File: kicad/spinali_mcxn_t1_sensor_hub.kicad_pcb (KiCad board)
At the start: 6 copper layers, 36.5 x 46 mm, 204 parts, among them J1 5055780421, J10 SDO, J11 CKO, J12 GND, J2 USB4105-GF-A, J3 CAN0A, J4 CAN0B, J5 Debug, J6 CAN1A, J7 CAN1B, J8 DF40TC(3.0)-50DP-0.4V(51), J9 DF40TC(3.0)-50DP-0.4V(51), Q1 BUK6D56-60EX, SW1 SW_SPST, U1 LM74700, U10 BMM350, U11 BMP581, U12 TJA1462ATK, U13 TJA1462ATK, U14 SK9822-EC20, U15 TJA1103AHN, U2 NX5P3363UKZ, U3 LM5160DNTJ, U4 NX5P3363UKZ, U5 MIC5504-1.8YMT, U6 MPM3811GG-Z, U7 MCXN947VDFT, U8 PCMF1USB3SZ, U9 ICM-45686, Y1 24MHz, Y2 32.768kHz, Y3 25MHz

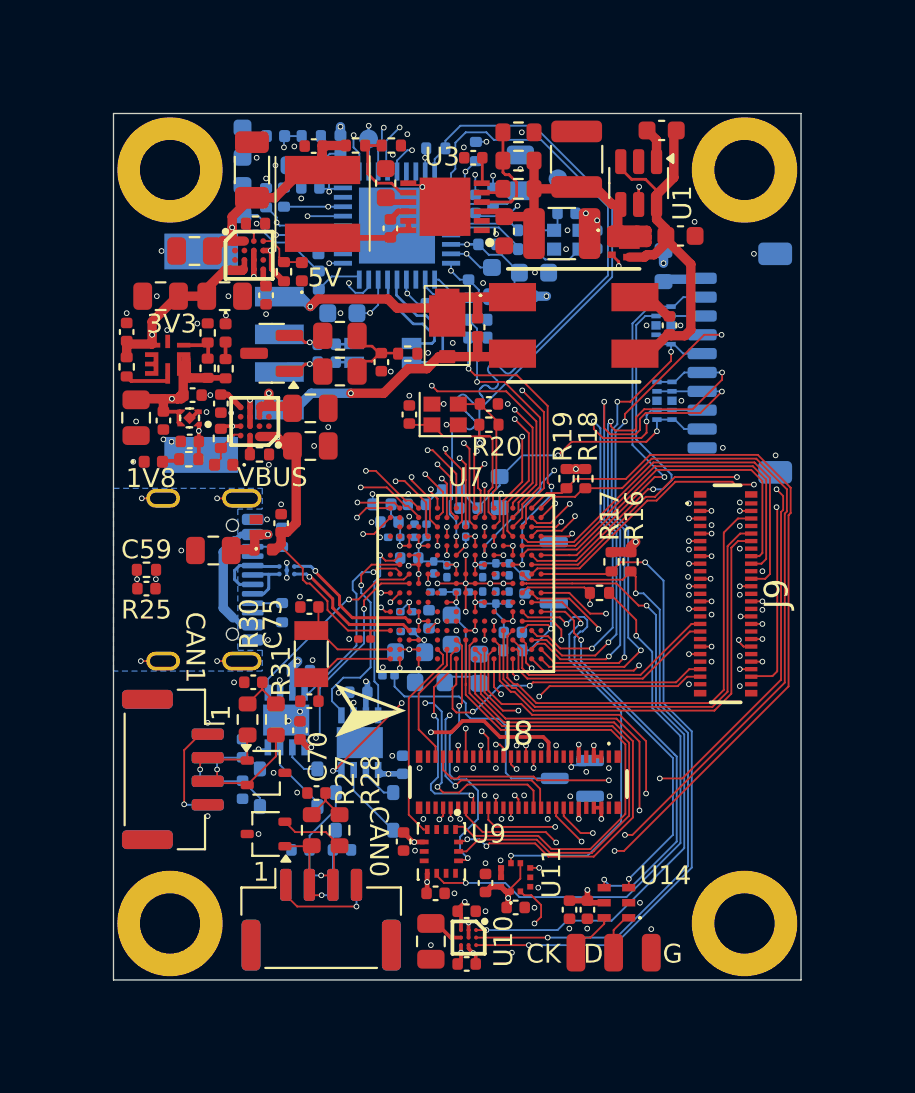
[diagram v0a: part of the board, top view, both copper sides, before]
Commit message: Updated layout and BOM
- Rounded corners of PCB
- Updated board-to-board MFPN to correct one.
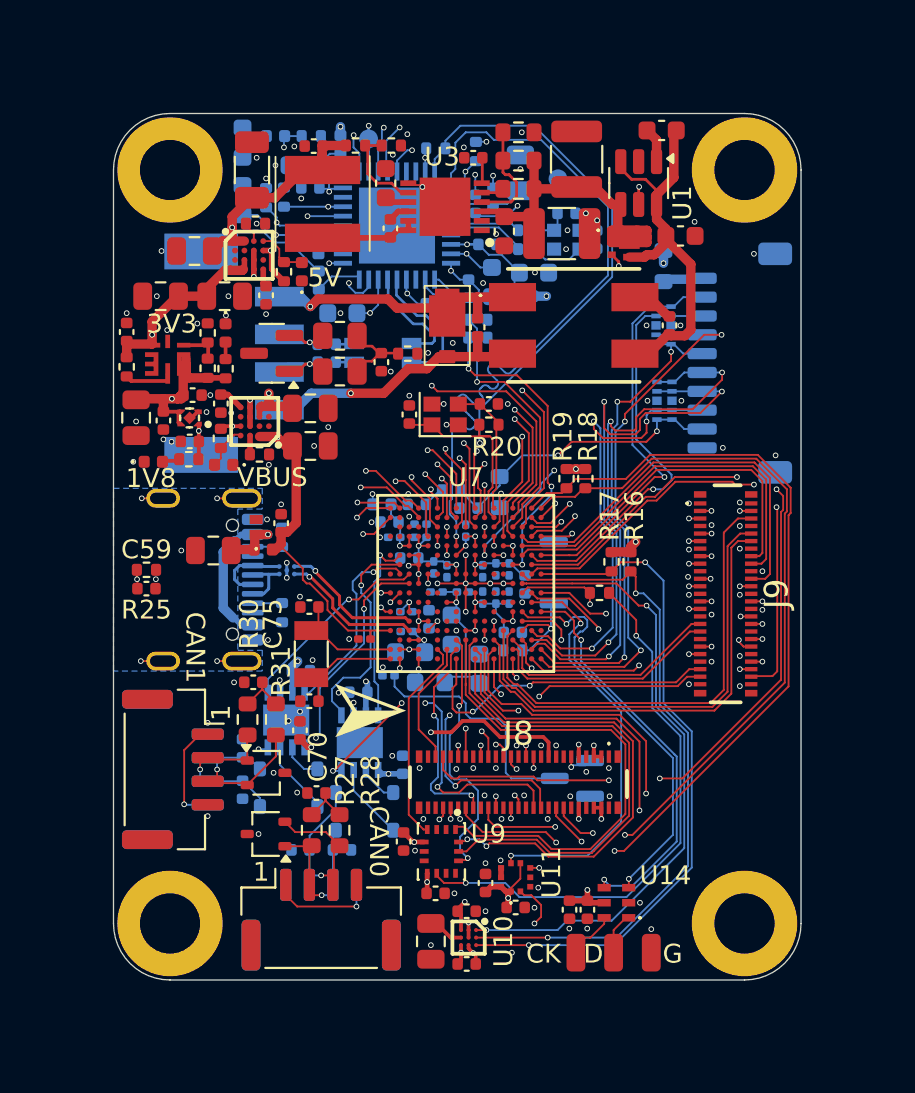
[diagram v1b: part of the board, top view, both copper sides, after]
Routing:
- net +1V8: track 48.1 -> 48.7 mm
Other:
- outline, holes or cut-outs redrawn
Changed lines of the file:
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@@
 		)
 	)
-	(gr_rect
-		(start 82.2 75.95)
-		(end 118.7 121.95)
+	(gr_arc
+		(start 82.2 78.95)
+		(mid 83.07868 76.82868)
+		(end 85.2 75.95)
+		(stroke
+			(width 0.05)
+			(type default)
+		)
+		(layer "Edge.Cuts")
+	)
+	(gr_line
+		(start 115.7 121.95)
+		(end 85.2 121.95)
+		(stroke
+			(width 0.05)
+			(type default)
+		)
+		(layer "Edge.Cuts")
+	)
+	(gr_arc
+		(start 85.2 121.95)
+		(mid 83.07868 121.07132)
+		(end 82.2 118.95)
+		(stroke
+			(width 0.05)
+			(type default)
+		)
+		(layer "Edge.Cuts")
+	)
+	(gr_line
+		(start 85.2 75.95)
+		(end 115.7 75.95)
+		(stroke
+			(width 0.05)
+			(type default)
+		)
+		(layer "Edge.Cuts")
+	)
+	(gr_arc
+		(start 115.7 75.95)
+		(mid 117.82132 76.82868)
+		(end 118.7 78.95)
+		(stroke
+			(width 0.05)
+			(type default)
+		)
+		(layer "Edge.Cuts")
+	)
+	(gr_line
+		(start 118.7 78.95)
+		(end 118.7 118.95)
+		(stroke
+			(width 0.05)
+			(type default)
+		)
+		(layer "Edge.Cuts")
+	)
+	(gr_arc
+		(start 118.7 118.95)
+		(mid 117.82132 121.07132)
+		(end 115.7 121.95)
+		(stroke
+			(width 0.05)
+			(type default)
+		)
+		(layer "Edge.Cuts")
+	)
+	(gr_line
+		(start 82.2 118.95)
+		(end 82.2 78.95)
 		(stroke
 			(width 0.05)
 			(type default)
 		)
-		(fill none)
 		(layer "Edge.Cuts")
 	)
@@
 	)
 	(segment
+		(start 97.25 109.5)
+		(end 97.5 109.5)
+		(width 0.2)
+		(layer "In2.Cu")
+		(net 8)
+	)
+	(segment
 		(start 100.25 116.734314)
 		(end 100.25 116.05)
@@
 	)
 	(segment
+		(start 97.5 109.7)
+		(end 97.5 109.5)
+		(width 0.2)
+		(layer "In2.Cu")
+		(net 8)
+	)
+	(segment
+		(start 97.5 113.3)
+		(end 97.5 109.7)
+		(width 0.2)
+		(layer "In2.Cu")
+		(net 8)
+	)
+	(segment
+		(start 97.7 109.5)
+		(end 97.5 109.5)
+		(width 0.2)
+		(layer "In2.Cu")
+		(net 8)
+	)
+	(segment
 		(start 87.15 94.55)
 		(end 87.15 105.55)
@@
 	(segment
 		(start 94.05 109.5)
-		(end 97.5 109.5)
+		(end 97.25 109.5)
+		(width 0.2)
+		(layer "In2.Cu")
+		(net 8)
+	)
+	(segment
+		(start 98.35 109.5)
+		(end 97.7 109.5)
 		(width 0.2)
 		(layer "In2.Cu")
@@
 	)
 	(segment
+		(start 97.5 109.7)
+		(end 97.3 109.5)
+		(width 0.2)
+		(layer "In2.Cu")
+		(net 8)
+	)
+	(segment
 		(start 87.15 105.55)
 		(end 90.25 108.65)
@@
 	)
 	(segment
-		(start 98.35 109.5)
-		(end 97.5 109.5)
+		(start 97.5 109.7)
+		(end 97.7 109.5)
+		(width 0.2)
+		(layer "In2.Cu")
+		(net 8)
+	)
+	(segment
+		(start 97.3 109.5)
+		(end 97.25 109.5)
 		(width 0.2)
 		(layer "In2.Cu")
@@
 	)
 	(segment
-		(start 97.5 113.3)
-		(end 97.5 109.5)
-		(width 0.2)
-		(layer "In2.Cu")
-		(net 8)
-	)
-	(segment
 		(start 93.2 108.65)
 		(end 94.05 109.5)
@@
 	)
 	(segment
-		(start 108.25 118.97)
-		(end 108.25 118.65)
-		(width 0.1)
-		(layer "F.Cu")
-		(net 224)
-	)
-	(segment
-		(start 107.2 119.7)
-		(end 107.52 119.7)
+		(start 107.52 119.7)
+		(end 108.25 118.97)
 		(width 0.1)
 		(layer "F.Cu")
@@
 	)
 	(segment
-		(start 106.75 120.5)
-		(end 106.75 120.15)
+		(start 108.25 118.97)
+		(end 108.25 118.65)
 		(width 0.1)
 		(layer "F.Cu")
@@
 	)
 	(segment
-		(start 107.52 119.7)
-		(end 108.25 118.97)
+		(start 107.2 119.7)
+		(end 107.52 119.7)
 		(width 0.1)
 		(layer "F.Cu")
@@
 	)
 	(segment
-		(start 108.25 118.97)
-		(end 108.25 118.9)
+		(start 106.75 120.15)
+		(end 107.2 119.7)
 		(width 0.1)
 		(layer "F.Cu")
@@
 	)
 	(segment
-		(start 106.75 120.15)
-		(end 107.2 119.7)
+		(start 106.75 120.5)
+		(end 106.75 120.15)
 		(width 0.1)
 		(layer "F.Cu")

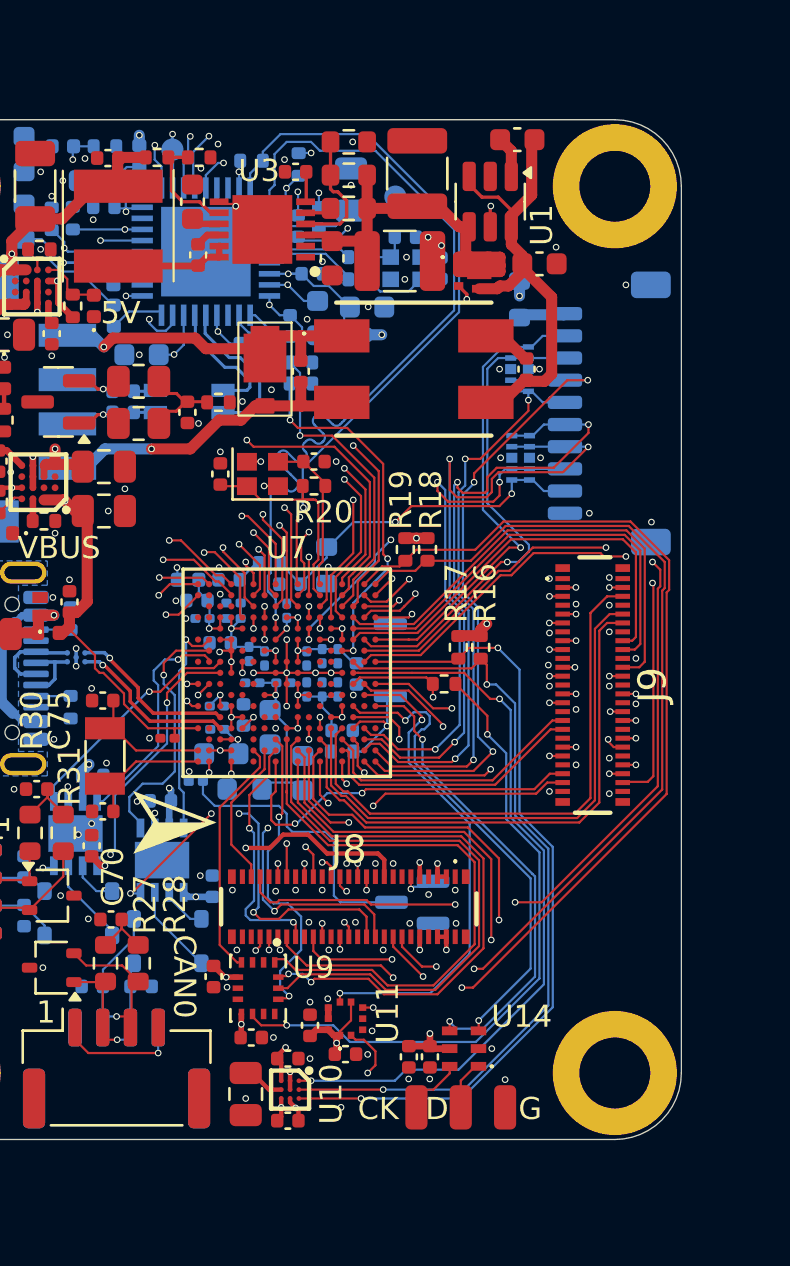
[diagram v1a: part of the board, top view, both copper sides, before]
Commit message: Updated PCB layout
- Changed North vector symbol on silk to an XYZ axis symbol.
- Flipped magnetometer to bottom side to have orientation match the IMU.
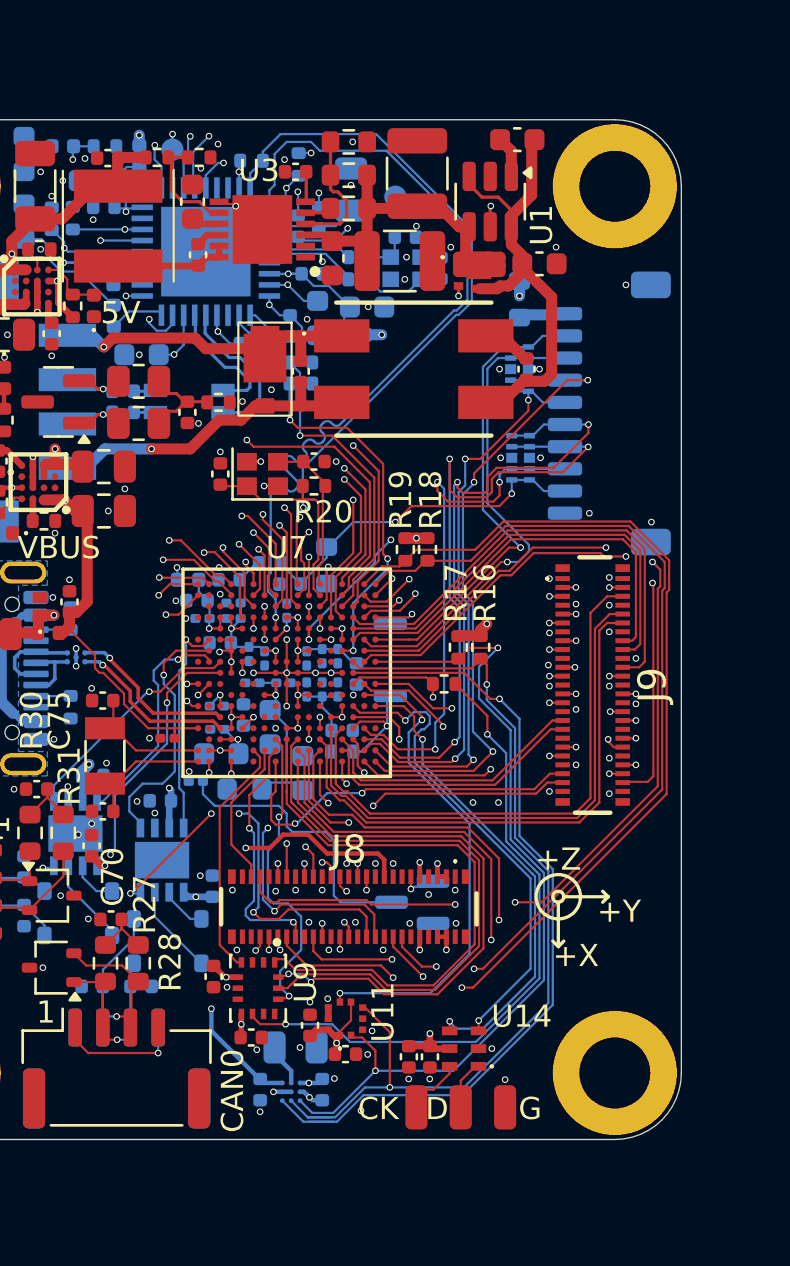
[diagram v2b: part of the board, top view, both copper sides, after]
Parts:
- removed the G*** at (95.8, 107.7)
- C62, C63, C64, U10: moved to B.Cu
- moved C64 3.08 mm to (101.3, 117.8), turned to 0 degrees
- moved C62 2.09 mm to (102.5, 119.7), turned to 90 degrees
- moved C63 1.88 mm to (99.7, 119.7), turned to -90 degrees
- moved U10 0.11 mm to (101.1, 119.8), turned to 0 degrees
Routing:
- net P0_19/BMM350_I2C_INT: track 33.6 -> 37.8 mm, vias 2 -> 1
- net P0_20/I3C0_SDA: track 40.4 -> 42.2 mm, vias 3 -> 2
- net P0_21/I3C0_SCL: track 40.0 -> 38.3 mm, vias 3 -> 2
- net P1_21/ENET0_MDIO: track 39.1 -> 39.9 mm
- net P1_20/ENET0_MDC: track 39.1 -> 38.3 mm
- net P0_4/DEBUG_GPIO: track 24.0 -> 23.4 mm
- net GND: vias 149 -> 152
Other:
- board text added: "+X"
- board text added: "+Y"
- board text added: "+Z"

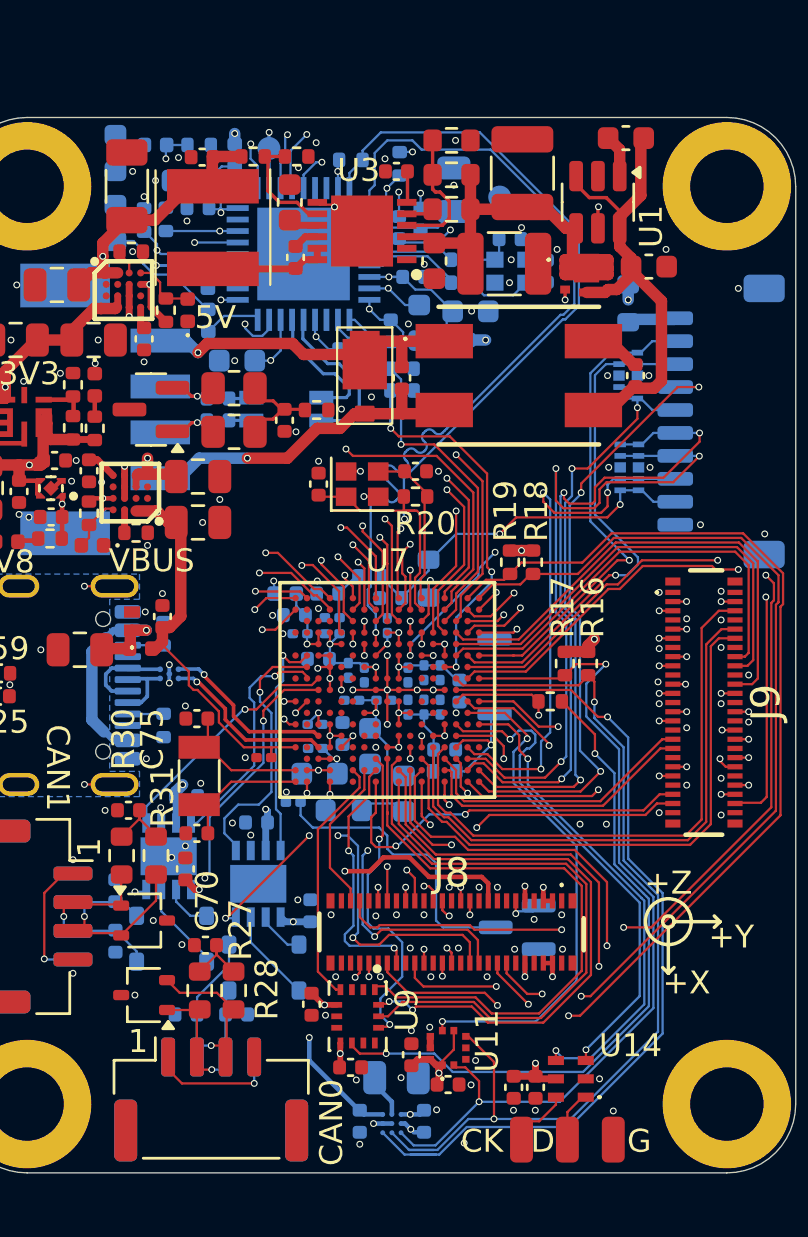
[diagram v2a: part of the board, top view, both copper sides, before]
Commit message: Updated layout and BOM
- Flipped Magnetometer so it is aligned with the axis of the IMU.
- Updated BOM so all parts can be sourced from DigiKey. Also added a row for JLCPCB part numbers if applicable.
- Replaced ISP button with the NanoT160AS. Added "ISP" in silkscreen at that button.
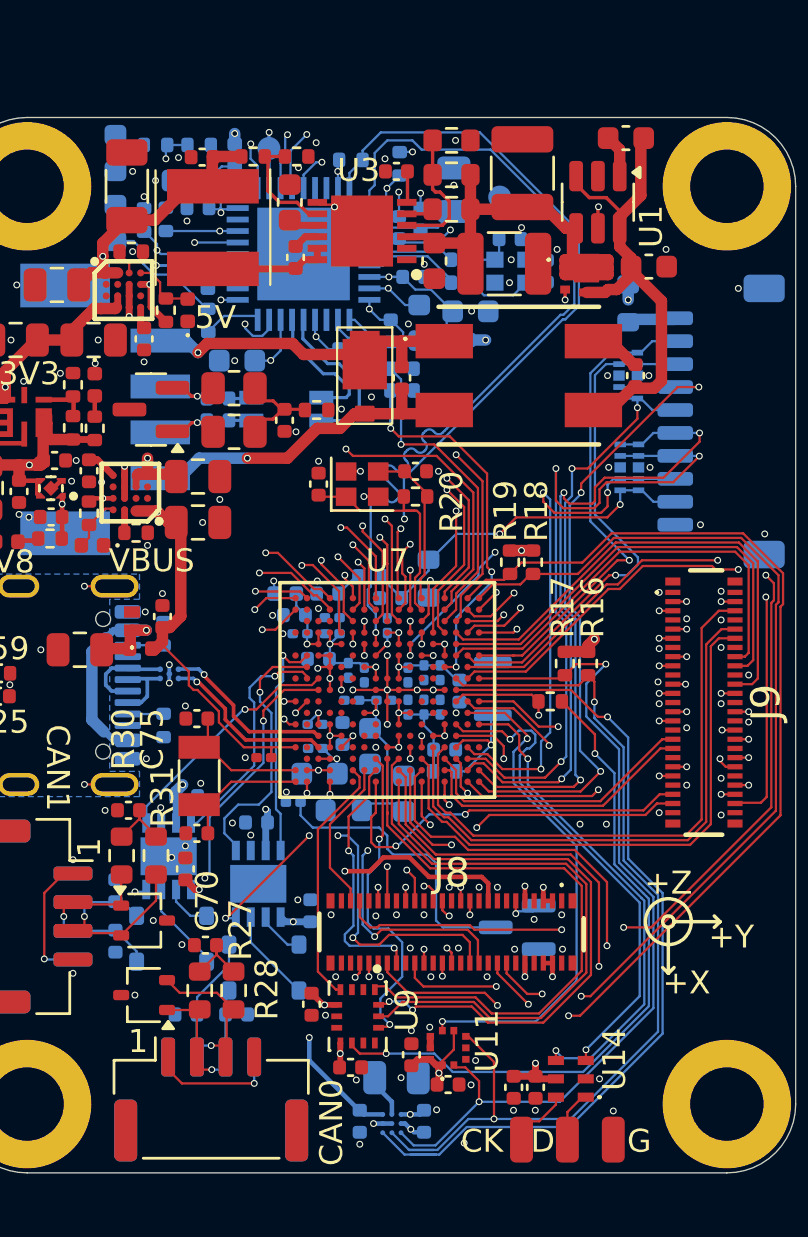
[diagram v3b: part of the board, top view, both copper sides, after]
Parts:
- R1, R6: value 2k2 -> 2k2 1%
- R37, R38: footprint Inductor_SMD:L_0402_1005Metric -> Resistor_SMD:R_0402_1005Metric
- SW1: value SW_SPST -> ISP; footprint Switches:TS2306A -> Switches:NanoTxxxAS
- moved SW1 0.53 mm to (105.5, 100.8)
